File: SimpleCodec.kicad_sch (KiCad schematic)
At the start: 7 parts, among them J1 RPI_ADC, J2 RP_GPIO

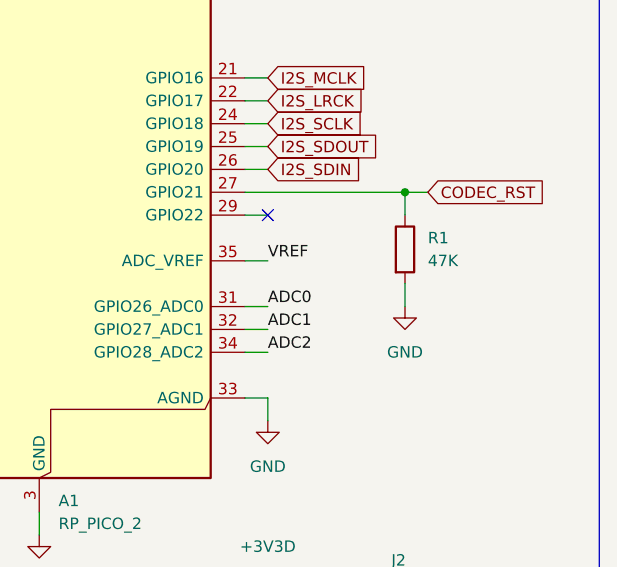
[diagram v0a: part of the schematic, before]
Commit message: Missing connections
Updated the board layout.
Added al missing connections.
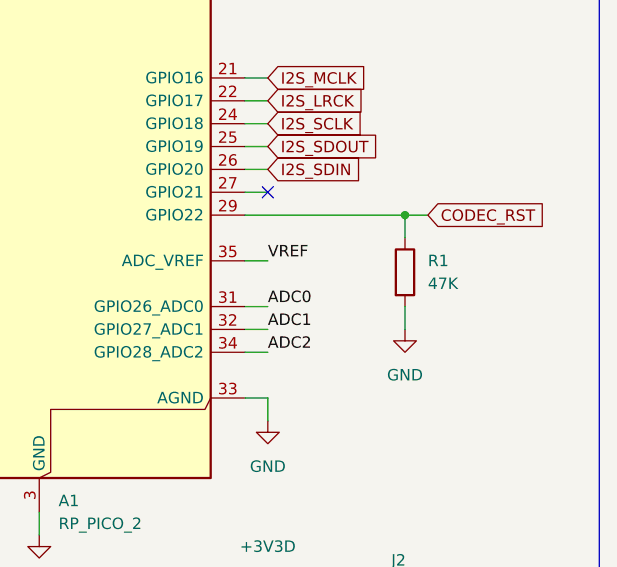
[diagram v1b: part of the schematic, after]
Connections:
- net CODEC_RST: now also A1.29 (GPIO22); no longer A1.27 (GPIO21)
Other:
- moved on the sheet: R1
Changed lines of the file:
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@@
 	)
 	(junction
-		(at 220.98 69.85)
+		(at 220.98 72.39)
 		(diameter 0)
 		(color 0 0 0 0)
@@
 	)
 	(no_connect
-		(at 205.74 72.39)
+		(at 205.74 69.85)
 	)
 	(wire
@@
 	(wire
 		(pts
-			(xy 223.52 69.85) (xy 220.98 69.85)
+			(xy 223.52 72.39) (xy 220.98 72.39)
 		)
 		(stroke
@@
 	(wire
 		(pts
+			(xy 203.2 69.85) (xy 205.74 69.85)
+		)
+		(stroke
+			(width 0)
+			(type default)
+		)
+	)
+	(wire
+		(pts
 			(xy 154.94 80.01) (xy 157.48 80.01)
 		)
@@
 	(wire
 		(pts
-			(xy 220.98 69.85) (xy 220.98 72.39)
+			(xy 220.98 72.39) (xy 220.98 74.93)
 		)
 		(stroke
@@
 	(wire
 		(pts
-			(xy 203.2 72.39) (xy 205.74 72.39)
-		)
-		(stroke
-			(width 0)
-			(type default)
-		)
-	)
-	(wire
-		(pts
-			(xy 203.2 69.85) (xy 220.98 69.85)
+			(xy 203.2 72.39) (xy 220.98 72.39)
 		)
 		(stroke
@@
 	(wire
 		(pts
-			(xy 220.98 80.01) (xy 220.98 82.55)
+			(xy 220.98 82.55) (xy 220.98 85.09)
 		)
 		(stroke
@@
 	(global_label "CODEC_RST"
 		(shape input)
-		(at 223.52 69.85 0)
+		(at 223.52 72.39 0)
 		(fields_autoplaced yes)
 		(effects
@@
 		)
 		(property "Intersheetrefs" "${INTERSHEET_REFS}"
-			(at 237.2094 69.85 0)
+			(at 237.2094 72.39 0)
 			(effects
 				(font
@@
 	(symbol
 		(lib_id "Device:R")
-		(at 220.98 76.2 0)
+		(at 220.98 78.74 0)
 		(unit 1)
 		(exclude_from_sim no)
@@
 		(dnp no)
 		(property "Reference" "R1"
-			(at 223.52 74.9299 0)
+			(at 223.52 77.4699 0)
 			(effects
 				(font
@@
 		)
 		(property "Value" "47K"
-			(at 223.52 77.4699 0)
+			(at 223.52 80.0099 0)
 			(effects
 				(font
@@
 		)
 		(property "Footprint" "Resistor_SMD:R_0603_1608Metric"
-			(at 219.202 76.2 90)
+			(at 219.202 78.74 90)
 			(effects
 				(font
@@
 		)
 		(property "Datasheet" "~"
-			(at 220.98 76.2 0)
+			(at 220.98 78.74 0)
 			(effects
 				(font
@@
 		)
 		(property "Description" "Resistor"
-			(at 220.98 76.2 0)
+			(at 220.98 78.74 0)
 			(effects
 				(font
@@
 	(symbol
 		(lib_id "power:GND")
-		(at 220.98 82.55 0)
+		(at 220.98 85.09 0)
 		(unit 1)
 		(exclude_from_sim no)
@@
 		(fields_autoplaced yes)
 		(property "Reference" "#PWR09"
-			(at 220.98 88.9 0)
+			(at 220.98 91.44 0)
 			(effects
 				(font
@@
 		)
 		(property "Value" "GND"
-			(at 220.98 87.63 0)
+			(at 220.98 90.17 0)
 			(effects
 				(font
@@
 		)
 		(property "Footprint" ""
-			(at 220.98 82.55 0)
+			(at 220.98 85.09 0)
 			(effects
 				(font
@@
 		)
 		(property "Datasheet" ""
-			(at 220.98 82.55 0)
+			(at 220.98 85.09 0)
 			(effects
 				(font
@@
 		)
 		(property "Description" "Power symbol creates a global label with name \"GND\" , ground"
-			(at 220.98 82.55 0)
-			(effects
-				(font
+			(at 220.98 85.09 0)
+			(effects
+				(font
